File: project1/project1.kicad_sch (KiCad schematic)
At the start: 4 parts, among them U1 TJA1050T, U2 MCP2515-xST, U3 STM32G474RBTx

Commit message: un début
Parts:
- added D1, D2: LED, symbol Device:LED
- added R1: R, symbol Device:R
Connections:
- net +5V: now also U3.1 (VBAT), D1.2 (A), D2.2 (A)
- net GND: now also R1.2
- net at U3.29 (VDDA): now also D2.1 (K)
- new net: D1.1 (K), R1.1

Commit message: avancements sur l'alimentation du STM32
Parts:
- removed D1, D2: LED, symbol Device:LED
- removed R1: R, symbol Device:R
- added C10, C8: 1uF, symbol Device:C
- added C2, C3, C5, C6, C9: 100nF, symbol Device:C
- added C4: 4.7uF, symbol Device:C
- added C7: 10nF, symbol Device:C
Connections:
- net +5V: no longer U3.1 (VBAT)
- net GND: now also U3.15 (VSS), U3.27 (VSSA), U3.31 (VSS), U3.47 (VSS), U3.63 (VSS), C10.2, C2.2, C3.2, C4.2, C5.2, C6.2, C7.2, C8.2, C9.2
- net +3.3V: now reaches U3.16 (VDD)
- net +3.3V: now also U3.1 (VBAT), U3.29 (VDDA), U3.32 (VDD), U3.48 (VDD), U3.64 (VDD), C2.1, C3.1, C4.1, C5.1, C6.1, C7.1, C8.1
- net at U3.28 (VREF+): now also C10.1, C9.1
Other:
- moved on the sheet: U2, U3

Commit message: changed CAN transceiver to SN65HVD23X
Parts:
- removed U1: TJA1050T, symbol exo-symbol-library:TJA1050T
- added C11, C12: 30pF, symbol Device:C
- added U4: SN65HVD230, Package_SO:SOIC-8_3.9x4.9mm_P1.27mm, symbol Interface_CAN_LIN:SN65HVD230
- added Y1: 8MHz, Exocet:Crystal_SMD_HC49-SD, symbol Exo_Symbol_Library:External_Oscillator
- C1: value 100nF -> 0.1uF
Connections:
- net +5V is gone; now on net +3.3V: C1.1
- net +3.3V: now also U4.3 (VCC)
- net GND: now also C11.2, C12.2, U4.2 (GND)
- net CAN_RX: now reaches U3.45 (PA11)
- net CAN_RX: now also U4.4 (R)
- net CAN_TX: now reaches U3.46 (PA12)
- net CAN_TX: now also U4.1 (D)
- net CAN_MODE: now reaches U3.49 (PA13)
- net CAN_MODE: now also U4.8 (Rs)
- net OSC_IN: now reaches U3.5 (PF0)
- net OSC_IN: now also C11.1, Y1.2
- net OSC_OUT: now reaches U3.6 (PF1)
- net OSC_OUT: now also C12.1, Y1.1
- new net CAN_H: U4.7 (CANH)
- new net CAN_L: U4.6 (CANL)
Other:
- note added: "CAN Tranceiver"
- note added: "High-speed external (HSE) oscillator"
- moved on the sheet: C10, C9, U2

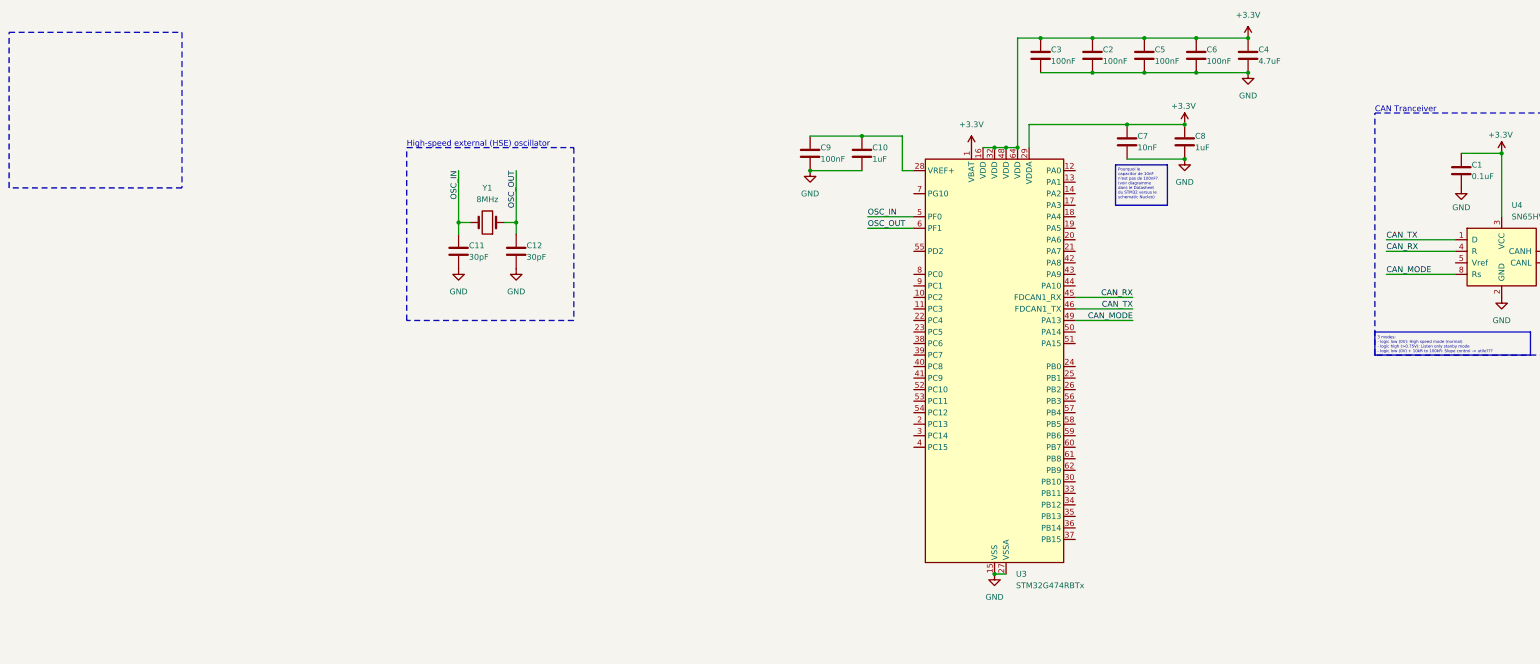
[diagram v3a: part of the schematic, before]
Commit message: mounting holes
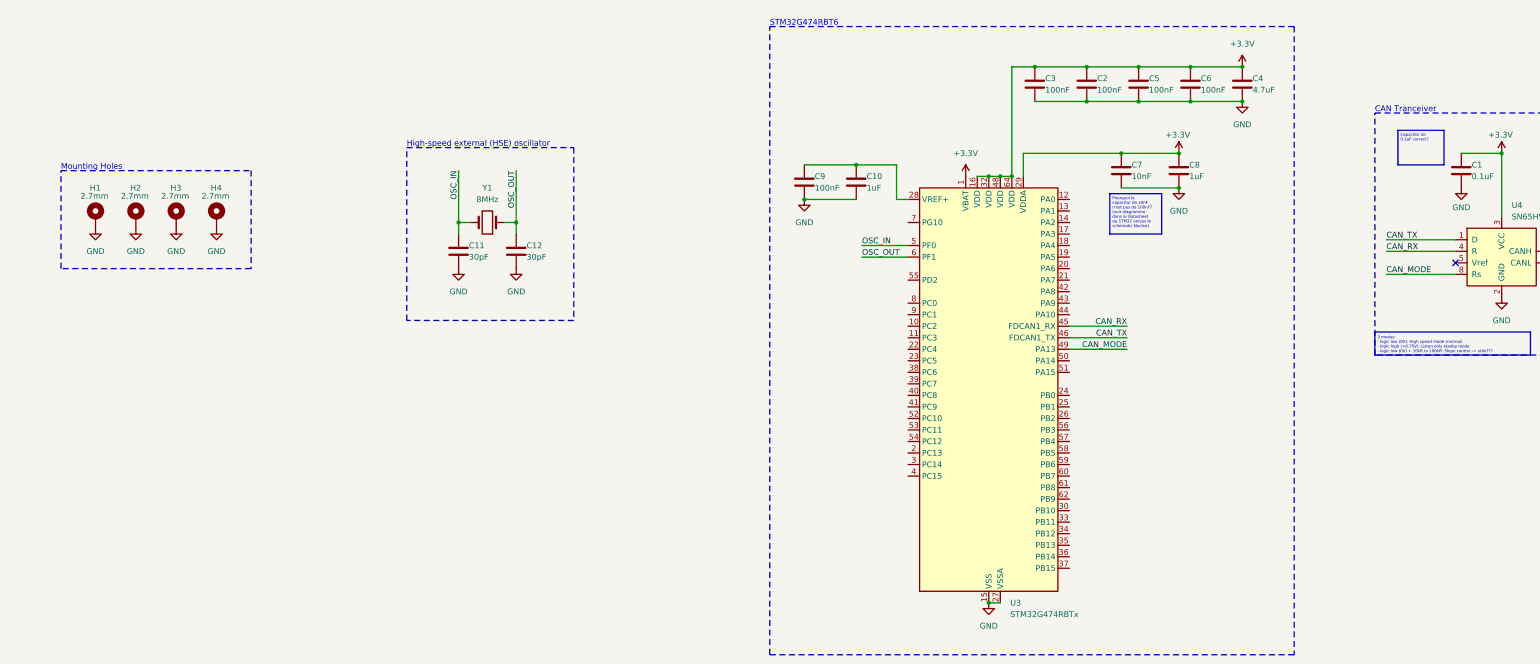
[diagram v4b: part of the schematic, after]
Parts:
- added H1, H2, H3, H4: 2.7mm, MountingHole:MountingHole_2.7mm_Pad, symbol Mechanical:MountingHole_Pad
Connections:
- net GND: now also H1.1, H2.1, H3.1, H4.1
- no-connect marks 0 -> 1
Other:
- note added: "Mounting Holes"
- note added: "STM32G474RBT6"
- moved on the sheet: C10, C2, C3, C4, C5, C6, C7, C8, C9, U3

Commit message: network connector
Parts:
- added J1: ~, symbol Exo_Symbol_Library:Network_Connector
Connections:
- net CAN_H: now also J1.3 (CAN_H)
- net CAN_L: now also J1.4 (CAN_L)
- net GND: now also J1.5 (GND)
- new net +24V: J1.1 (+24V)
- new net +5V: J1.2 (+5V)
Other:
- note added: "Network Connector"

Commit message: qqchose a été fait
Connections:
- net GND: now also C11.1, C12.1; no longer C11.2, C12.2
- net OSC_IN: now also C11.2, Y1.1; no longer C11.1, Y1.2
- net OSC_OUT: now also C12.2, Y1.2; no longer C12.1, Y1.1
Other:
- moved on the sheet: C11, C12, Y1
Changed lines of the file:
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@@
 	)
 	(junction
-		(at 118.11 66.04)
+		(at 128.27 59.69)
 		(diameter 0)
 		(color 0 0 0 0)
@@
 	)
 	(junction
-		(at 130.81 66.04)
+		(at 128.27 72.39)
 		(diameter 0)
 		(color 0 0 0 0)
@@
 	(wire
 		(pts
-			(xy 118.11 54.61) (xy 118.11 66.04)
-		)
-		(stroke
-			(width 0)
-			(type default)
-		)
-	)
-	(wire
-		(pts
-			(xy 118.11 68.58) (xy 118.11 66.04)
+			(xy 139.7 59.69) (xy 128.27 59.69)
+		)
+		(stroke
+			(width 0)
+			(type default)
+		)
+	)
+	(wire
+		(pts
+			(xy 125.73 59.69) (xy 128.27 59.69)
 		)
 		(stroke
@@
 	(wire
 		(pts
-			(xy 118.11 66.04) (xy 120.65 66.04)
+			(xy 128.27 59.69) (xy 128.27 62.23)
 		)
 		(stroke
@@
 	(wire
 		(pts
-			(xy 130.81 54.61) (xy 130.81 66.04)
+			(xy 139.7 72.39) (xy 128.27 72.39)
 		)
 		(stroke
@@
 	(wire
 		(pts
-			(xy 130.81 66.04) (xy 128.27 66.04)
+			(xy 128.27 72.39) (xy 128.27 69.85)
 		)
 		(stroke
@@
 	(wire
 		(pts
-			(xy 130.81 68.58) (xy 130.81 66.04)
+			(xy 125.73 72.39) (xy 128.27 72.39)
 		)
 		(stroke
@@
 	(rectangle
 		(start 106.68 49.53)
-		(end 143.51 87.63)
+		(end 144.78 83.82)
 		(stroke
 			(width 0)
@@
 	)
 	(label "OSC_OUT"
-		(at 130.81 54.61 270)
+		(at 139.7 72.39 180)
 		(fields_autoplaced yes)
 		(effects
@@
 	)
 	(label "OSC_IN"
-		(at 118.11 54.61 270)
+		(at 139.7 59.69 180)
 		(fields_autoplaced yes)
 		(effects
@@
 	(symbol
 		(lib_id "Device:C")
-		(at 130.81 72.39 0)
+		(at 121.92 72.39 90)
 		(unit 1)
 		(exclude_from_sim no)
@@
 		(dnp no)
 		(property "Reference" "C12"
-			(at 133.096 71.12 0)
+			(at 123.952 75.946 90)
 			(effects
 				(font
@@
 		)
 		(property "Value" "30pF"
-			(at 133.096 73.66 0)
+			(at 124.46 78.486 90)
 			(effects
 				(font
@@
 		)
 		(property "Footprint" ""
-			(at 131.7752 76.2 0)
+			(at 125.73 71.4248 0)
 			(effects
 				(font
@@
 		)
 		(property "Datasheet" "~"
-			(at 130.81 72.39 0)
+			(at 121.92 72.39 0)
 			(effects
 				(font
@@
 		)
 		(property "Description" "Unpolarized capacitor"
-			(at 130.81 72.39 0)
+			(at 121.92 72.39 0)
 			(effects
 				(font
@@
 	(symbol
 		(lib_id "Device:C")
-		(at 118.11 72.39 0)
+		(at 121.92 59.69 90)
 		(unit 1)
 		(exclude_from_sim no)
@@
 		(dnp no)
 		(property "Reference" "C11"
-			(at 120.396 71.12 0)
+			(at 123.952 53.594 90)
 			(effects
 				(font
@@
 		)
 		(property "Value" "30pF"
-			(at 120.396 73.66 0)
+			(at 123.952 56.134 90)
 			(effects
 				(font
@@
 		)
 		(property "Footprint" ""
-			(at 119.0752 76.2 0)
+			(at 125.73 58.7248 0)
 			(effects
 				(font
@@
 		)
 		(property "Datasheet" "~"
-			(at 118.11 72.39 0)
+			(at 121.92 59.69 0)
 			(effects
 				(font
@@
 		)
 		(property "Description" "Unpolarized capacitor"
-			(at 118.11 72.39 0)
+			(at 121.92 59.69 0)
 			(effects
 				(font
@@
 	(symbol
 		(lib_id "power:GND")
-		(at 130.81 76.2 0)
+		(at 118.11 72.39 270)
 		(unit 1)
 		(exclude_from_sim no)
@@
 		(fields_autoplaced yes)
 		(property "Reference" "#PWR012"
-			(at 130.81 82.55 0)
+			(at 111.76 72.39 0)
 			(effects
 				(font
@@
 		)
 		(property "Value" "GND"
-			(at 130.81 81.28 0)
+			(at 113.03 72.39 0)
 			(effects
 				(font
@@
 		)
 		(property "Footprint" ""
-			(at 130.81 76.2 0)
+			(at 118.11 72.39 0)
 			(effects
 				(font
@@
 		)
 		(property "Datasheet" ""
-			(at 130.81 76.2 0)
+			(at 118.11 72.39 0)
 			(effects
 				(font
@@
 		)
 		(property "Description" "Power symbol creates a global label with name \"GND\" , ground"
-			(at 130.81 76.2 0)
+			(at 118.11 72.39 0)
 			(effects
 				(font
@@
 	(symbol
 		(lib_id "Exo_Symbol_Library:External_Oscillator")
-		(at 124.46 66.04 180)
+		(at 128.27 66.04 270)
 		(unit 1)
 		(exclude_from_sim no)
@@
 		(fields_autoplaced yes)
 		(property "Reference" "Y1"
-			(at 124.46 58.42 0)
-			(effects
-				(font
-					(size 1.27 1.27)
-				)
+			(at 132.08 64.7699 90)
+			(effects
+				(font
+					(size 1.27 1.27)
+				)
+				(justify left)
 			)
 		)
 		(property "Value" "8MHz"
-			(at 124.46 60.96 0)
-			(effects
-				(font
-					(size 1.27 1.27)
-				)
+			(at 132.08 67.3099 90)
+			(effects
+				(font
+					(size 1.27 1.27)
+				)
+				(justify left)
 			)
 		)
 		(property "Footprint" "Exocet:Crystal_SMD_HC49-SD"
-			(at 124.46 66.04 0)
+			(at 128.27 66.04 0)
 			(effects
 				(font
@@
 		)
 		(property "Datasheet" "~"
-			(at 124.46 66.04 0)
+			(at 128.27 66.04 0)
 			(effects
 				(font
@@
 		)
 		(property "Description" "Two pin crystal"
-			(at 124.46 66.04 0)
+			(at 128.27 66.04 0)
 			(effects
 				(font
@@
 		)
 		(property "JLCPCB" "C12674"
-			(at 124.46 66.04 0)
+			(at 128.27 66.04 0)
 			(effects
 				(font
@@
 		)
 		(property "Part Name" "X49SM8MSD2SC"
-			(at 124.46 66.04 0)
+			(at 128.27 66.04 0)
 			(effects
 				(font
@@
 	(symbol
 		(lib_id "power:GND")
-		(at 118.11 76.2 0)
+		(at 118.11 59.69 270)
 		(unit 1)
 		(exclude_from_sim no)
@@
 		(fields_autoplaced yes)
 		(property "Reference" "#PWR011"
-			(at 118.11 82.55 0)
+			(at 111.76 59.69 0)
 			(effects
 				(font
@@
 		)
 		(property "Value" "GND"
-			(at 118.11 81.28 0)
+			(at 113.03 59.69 0)
 			(effects
 				(font
@@
 		)
 		(property "Footprint" ""
-			(at 118.11 76.2 0)
+			(at 118.11 59.69 0)
 			(effects
 				(font
@@
 		)
 		(property "Datasheet" ""
-			(at 118.11 76.2 0)
+			(at 118.11 59.69 0)
 			(effects
 				(font
@@
 		)
 		(property "Description" "Power symbol creates a global label with name \"GND\" , ground"
-			(at 118.11 76.2 0)
-			(effects
-				(font
+			(at 118.11 59.69 0)
+			(effects
+				(font
